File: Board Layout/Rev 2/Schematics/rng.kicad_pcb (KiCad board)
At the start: 2 copper layers, 12 parts, among them P1 CONN_1, P2 CONN_1, P3 CONN_1, Q1 NPN, Q2 NPN, Q3 NPN

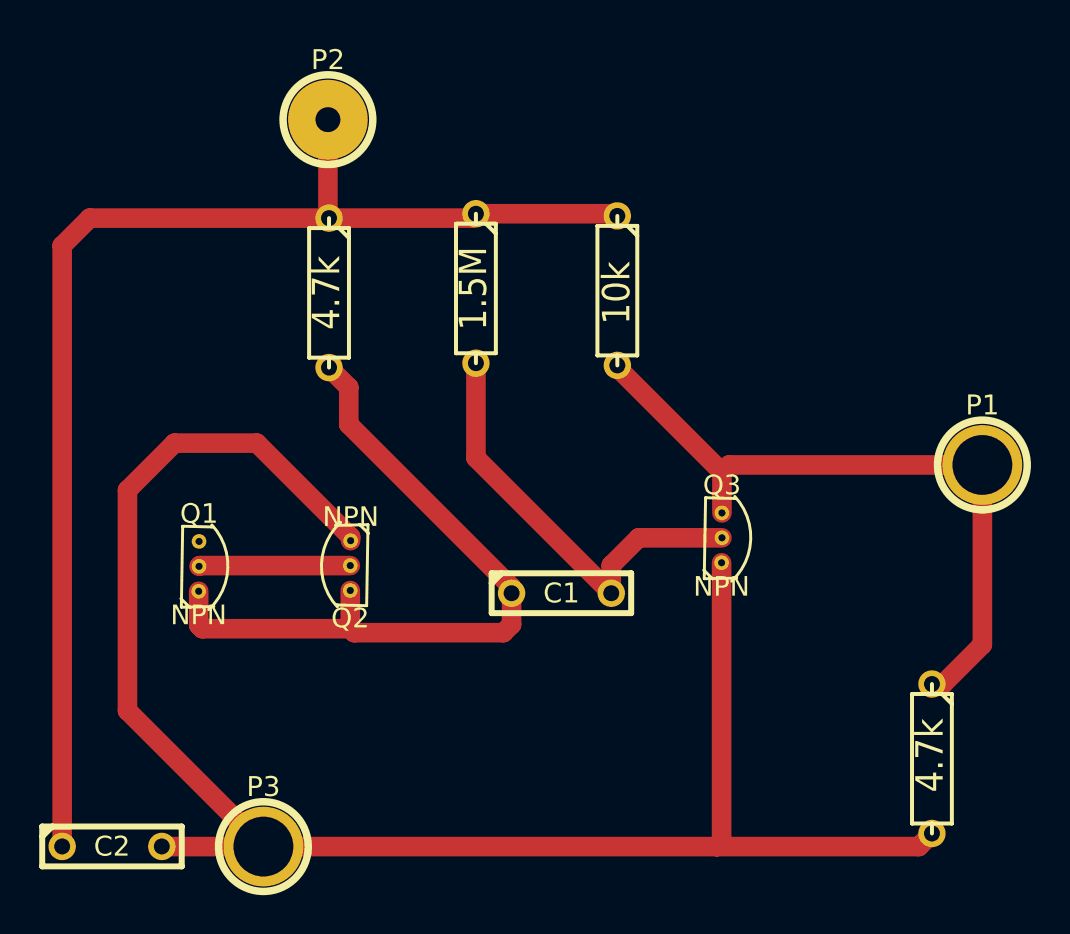
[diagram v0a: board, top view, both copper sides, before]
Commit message: Board Completion
RNG is complete, -  Trace widths much larger, condusive to self etching.
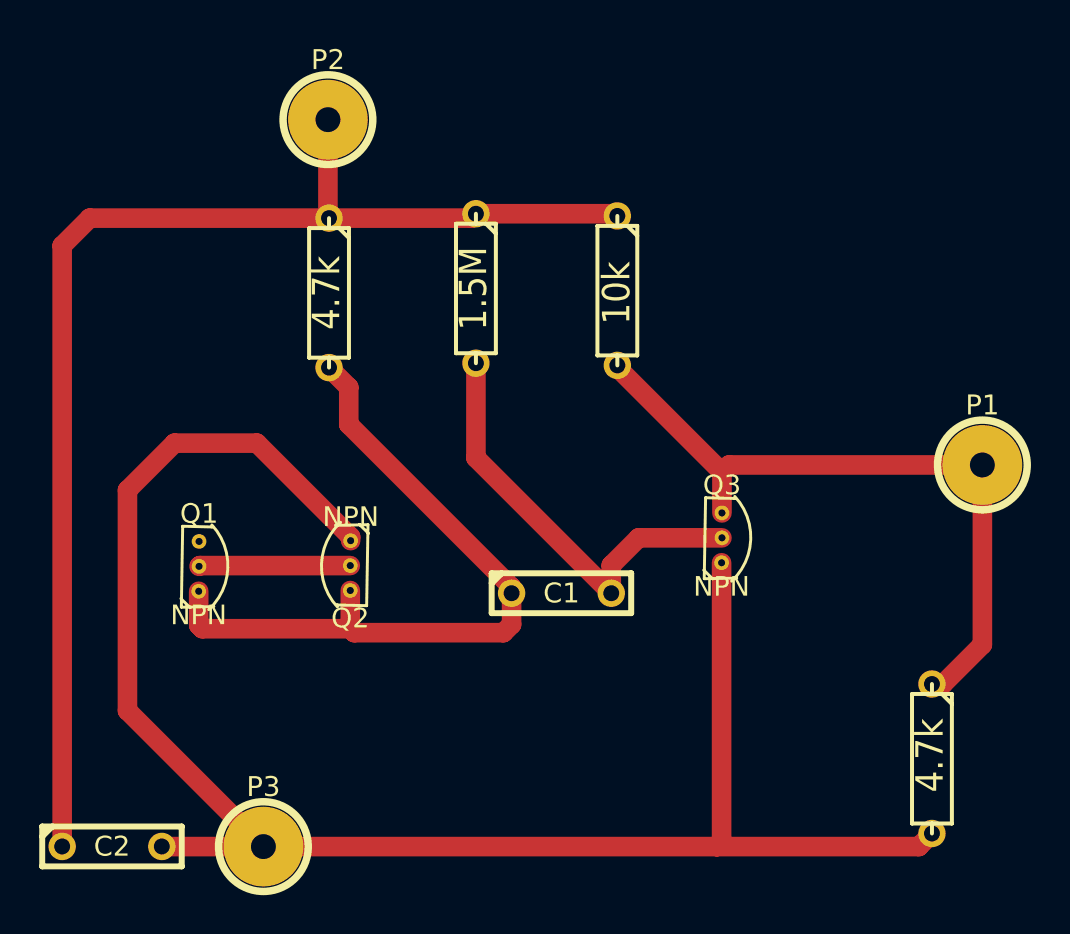
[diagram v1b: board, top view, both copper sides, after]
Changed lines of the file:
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@@
     (links 17)
     (no_connects 0)
-    (area 180.273959 132.29844 232.372746 176.59604)
+    (area 180.273959 132.29844 232.372746 176.9745)
     (thickness 1.6)
     (drawings 0)
@@
     (visible_elements 7FFFFFFF)
     (pcbplotparams
-      (layerselection 3178497)
+      (layerselection 32768)
       (usegerberextensions true)
       (excludeedgelayer true)
@@
       (outputformat 1)
       (mirror false)
-      (drillshape 1)
+      (drillshape 0)
       (scaleselection 1)
-      (outputdirectory ""))
+      (outputdirectory ../Gerbers/))
   )
   (net 0 "")
@@
     )
     (fp_circle (center 0 0) (end 0 -2.286) (layer F.SilkS) (width 0.381))
-    (pad 1 thru_hole circle (at 0 0) (size 4.064 4.064) (drill 3.048)
+    (pad 1 thru_hole circle (at 0 0) (size 4.064 4.064) (drill 1.27)
       (layers *.Cu *.Mask F.SilkS)
       (net 5 N-000006)
@@
     )
     (fp_circle (center 0 0) (end 0 -2.286) (layer F.SilkS) (width 0.381))
-    (pad 1 thru_hole circle (at 0 0) (size 4.064 4.064) (drill 3.048)
+    (pad 1 thru_hole circle (at 0 0) (size 4.064 4.064) (drill 1.27)
       (layers *.Cu *.Mask F.SilkS)
       (net 1 N-000001)
@@
     )
   )
-  (segment (start 196.40169 157.69717) (end 196.40169 157.50169) (width 1) (layer F.Cu) (net 1) (status C00000))
-  (segment (start 185.025 166.36108) (end 191.95542 173.2915) (width 1) (layer F.Cu) (net 1) (status 800000))
+  (segment (start 196.40169 157.69717) (end 196.40169 157.50169) (width 1) (layer F.Cu) (net 1))
+  (segment (start 185.025 166.36108) (end 191.95542 173.2915) (width 1) (layer F.Cu) (net 1))
   (segment (start 185.025 155.125) (end 185.025 166.36108) (width 1) (layer F.Cu) (net 1))
   (segment (start 187.425 152.725) (end 185.025 155.125) (width 1) (layer F.Cu) (net 1))
   (segment (start 191.625 152.725) (end 187.425 152.725) (width 1) (layer F.Cu) (net 1))
-  (segment (start 196.40169 157.50169) (end 191.625 152.725) (width 1) (layer F.Cu) (net 1) (status 400000))
-  (segment (start 215.31199 158.82239) (end 215.31199 173.05401) (width 1) (layer F.Cu) (net 1) (status 400000))
+  (segment (start 196.40169 157.50169) (end 191.625 152.725) (width 1) (layer F.Cu) (net 1))
+  (segment (start 215.31199 158.82239) (end 215.31199 173.05401) (width 1) (layer F.Cu) (net 1))
   (segment (start 215.31199 173.05401) (end 215.0745 173.2915) (width 1) (layer F.Cu) (net 1))
-  (segment (start 191.95542 173.2915) (end 215.0745 173.2915) (width 1) (layer F.Cu) (net 1) (status 400000))
+  (segment (start 191.95542 173.2915) (end 215.0745 173.2915) (width 1) (layer F.Cu) (net 1))
   (segment (start 215.0745 173.2915) (end 225.36658 173.2915) (width 1) (layer F.Cu) (net 1))
-  (segment (start 225.36658 173.2915) (end 226.0346 172.62348) (width 1) (layer F.Cu) (net 1) (status 800000))
-  (segment (start 191.95542 173.2915) (end 186.78398 173.2915) (width 1) (layer F.Cu) (net 1) (status C00000))
-  (segment (start 186.78398 173.2915) (end 186.77636 173.28388) (width 1) (layer F.Cu) (net 1) (status C00000))
-  (segment (start 196.38391 158.96717) (end 188.71311 158.96717) (width 1) (layer F.Cu) (net 2) (status C00000))
-  (segment (start 188.71311 158.96717) (end 188.67501 159.00527) (width 1) (layer F.Cu) (net 2) (status C00000))
-  (segment (start 204.60716 160.3756) (end 204.60716 160.0708) (width 1) (layer F.Cu) (net 3) (status C00000))
-  (segment (start 196.30644 149.88032) (end 195.3006 148.87448) (width 1) (layer F.Cu) (net 3) (status 800000))
+  (segment (start 225.36658 173.2915) (end 226.0346 172.62348) (width 1) (layer F.Cu) (net 1))
+  (segment (start 191.95542 173.2915) (end 186.78398 173.2915) (width 1) (layer F.Cu) (net 1))
+  (segment (start 186.78398 173.2915) (end 186.77636 173.28388) (width 1) (layer F.Cu) (net 1))
+  (segment (start 196.38391 158.96717) (end 188.71311 158.96717) (width 1) (layer F.Cu) (net 2))
+  (segment (start 188.71311 158.96717) (end 188.67501 159.00527) (width 1) (layer F.Cu) (net 2))
+  (segment (start 204.60716 160.3756) (end 204.60716 160.0708) (width 1) (layer F.Cu) (net 3))
+  (segment (start 196.30644 149.88032) (end 195.3006 148.87448) (width 1) (layer F.Cu) (net 3))
   (segment (start 196.30644 151.77008) (end 196.30644 149.88032) (width 1) (layer F.Cu) (net 3))
-  (segment (start 204.60716 160.0708) (end 196.30644 151.77008) (width 1) (layer F.Cu) (net 3) (status 400000))
-  (segment (start 188.65723 160.27527) (end 188.65723 162.00247) (width 1) (layer F.Cu) (net 3) (status 400000))
+  (segment (start 204.60716 160.0708) (end 196.30644 151.77008) (width 1) (layer F.Cu) (net 3))
+  (segment (start 188.65723 160.27527) (end 188.65723 162.00247) (width 1) (layer F.Cu) (net 3))
   (segment (start 188.84011 162.18535) (end 196.38391 162.18535) (width 1) (layer F.Cu) (net 3))
   (segment (start 188.65723 162.00247) (end 188.84011 162.18535) (width 1) (layer F.Cu) (net 3))
-  (segment (start 204.60716 160.3756) (end 204.60716 161.97072) (width 1) (layer F.Cu) (net 3) (status 400000))
-  (segment (start 196.38391 162.18535) (end 196.38391 160.23717) (width 1) (layer F.Cu) (net 3) (status 800000))
+  (segment (start 204.60716 160.3756) (end 204.60716 161.97072) (width 1) (layer F.Cu) (net 3))
+  (segment (start 196.38391 162.18535) (end 196.38391 160.23717) (width 1) (layer F.Cu) (net 3))
   (segment (start 196.58584 162.38728) (end 196.38391 162.18535) (width 1) (layer F.Cu) (net 3))
   (segment (start 204.1906 162.38728) (end 196.58584 162.38728) (width 1) (layer F.Cu) (net 3))
   (segment (start 204.60716 161.97072) (end 204.1906 162.38728) (width 1) (layer F.Cu) (net 3))
-  (segment (start 215.32977 157.55239) (end 211.08543 157.55239) (width 1) (layer F.Cu) (net 4) (status 400000))
-  (segment (start 209.68716 158.95066) (end 209.68716 160.3756) (width 1) (layer F.Cu) (net 4) (status 800000))
+  (segment (start 215.32977 157.55239) (end 211.08543 157.55239) (width 1) (layer F.Cu) (net 4))
+  (segment (start 209.68716 158.95066) (end 209.68716 160.3756) (width 1) (layer F.Cu) (net 4))
   (segment (start 211.08543 157.55239) (end 209.68716 158.95066) (width 1) (layer F.Cu) (net 4))
-  (segment (start 202.78852 148.65096) (end 202.78852 153.47696) (width 1) (layer F.Cu) (net 4) (status 400000))
-  (segment (start 202.78852 153.47696) (end 209.68716 160.3756) (width 1) (layer F.Cu) (net 4) (status 800000))
-  (segment (start 209.99704 148.76272) (end 209.99704 148.8694) (width 1) (layer F.Cu) (net 5) (status C00000))
-  (segment (start 209.99704 148.8694) (end 215.32977 154.20213) (width 1) (layer F.Cu) (net 5) (status 400000))
-  (segment (start 215.32977 156.28239) (end 215.32977 154.20213) (width 1) (layer F.Cu) (net 5) (status 400000))
-  (segment (start 215.69426 153.83764) (end 228.60508 153.83764) (width 1) (layer F.Cu) (net 5) (status 800000))
+  (segment (start 202.78852 148.65096) (end 202.78852 153.47696) (width 1) (layer F.Cu) (net 4))
+  (segment (start 202.78852 153.47696) (end 209.68716 160.3756) (width 1) (layer F.Cu) (net 4))
+  (segment (start 209.99704 148.76272) (end 209.99704 148.8694) (width 1) (layer F.Cu) (net 5))
+  (segment (start 209.99704 148.8694) (end 215.32977 154.20213) (width 1) (layer F.Cu) (net 5))
+  (segment (start 215.32977 156.28239) (end 215.32977 154.20213) (width 1) (layer F.Cu) (net 5))
+  (segment (start 215.69426 153.83764) (end 228.60508 153.83764) (width 1) (layer F.Cu) (net 5))
   (segment (start 215.32977 154.20213) (end 215.69426 153.83764) (width 1) (layer F.Cu) (net 5))
-  (segment (start 226.0346 165.00348) (end 226.60102 165.00348) (width 1) (layer F.Cu) (net 5) (status C00000))
-  (segment (start 228.60508 162.99942) (end 228.60508 153.83764) (width 1) (layer F.Cu) (net 5) (status 800000))
-  (segment (start 226.60102 165.00348) (end 228.60508 162.99942) (width 1) (layer F.Cu) (net 5) (status 400000))
-  (segment (start 181.69636 173.28388) (end 181.69636 142.66164) (width 1) (layer F.Cu) (net 6) (status 400000))
-  (segment (start 183.10352 141.25448) (end 195.3006 141.25448) (width 1) (layer F.Cu) (net 6) (status 800000))
+  (segment (start 226.0346 165.00348) (end 226.60102 165.00348) (width 1) (layer F.Cu) (net 5))
+  (segment (start 228.60508 162.99942) (end 228.60508 153.83764) (width 1) (layer F.Cu) (net 5))
+  (segment (start 226.60102 165.00348) (end 228.60508 162.99942) (width 1) (layer F.Cu) (net 5))
+  (segment (start 181.69636 173.28388) (end 181.69636 142.66164) (width 1) (layer F.Cu) (net 6))
+  (segment (start 183.10352 141.25448) (end 195.3006 141.25448) (width 1) (layer F.Cu) (net 6))
   (segment (start 181.69636 142.66164) (end 183.10352 141.25448) (width 1) (layer F.Cu) (net 6))
-  (segment (start 195.24472 136.23544) (end 195.24472 141.1986) (width 1) (layer F.Cu) (net 6) (status C00000))
-  (segment (start 195.24472 141.1986) (end 195.3006 141.25448) (width 1) (layer F.Cu) (net 6) (status C00000))
-  (segment (start 202.78852 141.03096) (end 209.88528 141.03096) (width 1) (layer F.Cu) (net 6) (status C00000))
-  (segment (start 209.88528 141.03096) (end 209.99704 141.14272) (width 1) (layer F.Cu) (net 6) (status C00000))
-  (segment (start 195.3006 141.25448) (end 202.565 141.25448) (width 1) (layer F.Cu) (net 6) (status C00000))
-  (segment (start 202.565 141.25448) (end 202.78852 141.03096) (width 1) (layer F.Cu) (net 6) (status C00000))
+  (segment (start 195.24472 136.23544) (end 195.24472 141.1986) (width 1) (layer F.Cu) (net 6))
+  (segment (start 195.24472 141.1986) (end 195.3006 141.25448) (width 1) (layer F.Cu) (net 6))
+  (segment (start 202.78852 141.03096) (end 209.88528 141.03096) (width 1) (layer F.Cu) (net 6))
+  (segment (start 209.88528 141.03096) (end 209.99704 141.14272) (width 1) (layer F.Cu) (net 6))
+  (segment (start 195.3006 141.25448) (end 202.565 141.25448) (width 1) (layer F.Cu) (net 6))
+  (segment (start 202.565 141.25448) (end 202.78852 141.03096) (width 1) (layer F.Cu) (net 6))
 )
